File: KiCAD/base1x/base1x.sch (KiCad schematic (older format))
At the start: 39 parts, among them J1 Conn_02x05_Odd_Even, J2 GS3, J3 Conn_02x14_Counter_Clockwise, J4 GS3, J6 Conn_02x14_Counter_Clockwise, J7 Conn_02x06_Counter_Clockwise, J8 Conn_02x06_Counter_Clockwise, J9 Screw_Terminal_01x08, P3 CONN_01X02, P4 CONN_01X02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

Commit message: update kicad and add logos
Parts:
- J9: symbol Connector_Specialized:Screw_Terminal_01x08 -> Connector:Screw_Terminal_01x08
- L1: value GREY@CHRISTOFORO.NET -> grey@mutovis.com; footprint myParts:logo -> logo:logo_and_text; symbol myParts:GREY@CHRISTOFORO.NET -> logo:logo_text
- MK1, MK2: symbol Mechanical:Mounting_Hole_PAD -> Mechanical:MountingHole_Pad
- MK3, MK4, MK5, MK6, MK7, MK8: symbol Mechanical:Mounting_Hole -> Mechanical:MountingHole_Pad
- TP1, TP2, TP3, TP4, TP5, TP6: symbol Connector_Specialized:Test_Point -> Connector:TestPoint
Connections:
- no-connect marks 35 -> 41
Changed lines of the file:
@@
 V+
 $Comp
-L myParts:GREY@CHRISTOFORO.NET L1
+L logo:logo_text L1
 U 1 1 59B41702
-P 8950 7250
-F 0 "L1" H 8950 7125 60  0001 C CNN
-F 1 "GREY@CHRISTOFORO.NET" H 8950 7250 100 0000 C CNB
-F 2 "myParts:logo" H 8950 7250 60  0001 C CNN
-F 3 "" H 8950 7250 60  0001 C CNN
-	1    8950 7250
+P 9050 6800
+F 0 "L1" H 9050 6675 60  0001 C CNN
+F 1 "grey@mutovis.com" H 9000 6550 100 0000 C CNN
+F 2 "logo:logo_and_text" H 9050 6800 60  0001 C CNN
+F 3 "" H 9050 6800 60  0001 C CNN
+	1    9050 6800
 	1    0    0    -1
 $EndComp
@@
 External Power
 $Comp
-L Mechanical:Mounting_Hole_PAD MK1
+L Mechanical:MountingHole_Pad MK1
 U 1 1 59C916FE
 P 3300 6100
@@
 $EndComp
 $Comp
-L Mechanical:Mounting_Hole_PAD MK2
+L Mechanical:MountingHole_Pad MK2
 U 1 1 59C91760
 P 3300 6450
@@
 V_D_EXT
 $Comp
-L Connector_Specialized:Test_Point TP1
+L Connector:TestPoint TP1
 U 1 1 5A00C70E
 P 5650 6300
@@
 ~CS0
 $Comp
-L Connector_Specialized:Test_Point TP2
+L Connector:TestPoint TP2
 U 1 1 5A00C0AD
 P 4700 1850
@@
 I-R
 $Comp
-L Mechanical:Mounting_Hole MK3
+L Mechanical:MountingHole_Pad MK3
 U 1 1 5A00CBDC
 P 8800 1700
@@
 $EndComp
 $Comp
-L Mechanical:Mounting_Hole MK4
+L Mechanical:MountingHole_Pad MK4
 U 1 1 5A00CCA4
 P 8800 2050
@@
 $EndComp
 $Comp
-L Mechanical:Mounting_Hole MK5
+L Mechanical:MountingHole_Pad MK5
 U 1 1 5A00CCFE
 P 8800 2350
@@
 $EndComp
 $Comp
-L Mechanical:Mounting_Hole MK6
+L Mechanical:MountingHole_Pad MK6
 U 1 1 5A00CD58
 P 8800 2650
@@
 $EndComp
 $Comp
-L Mechanical:Mounting_Hole MK7
+L Mechanical:MountingHole_Pad MK7
 U 1 1 5A00CDAE
 P 8800 3000
@@
 $EndComp
 $Comp
-L Mechanical:Mounting_Hole MK8
+L Mechanical:MountingHole_Pad MK8
 U 1 1 5A00CE0E
 P 8800 3300
@@
 	4700 6750 4700 6450
 $Comp
-L Connector_Specialized:Screw_Terminal_01x08 J9
+L Connector:Screw_Terminal_01x08 J9
 U 1 1 5A36A6E7
 P 10150 1350
@@
 NoConn ~ 10050 1150
 $Comp
-L Connector_Specialized:Test_Point TP3
+L Connector:TestPoint TP3
 U 1 1 5A3700D5
 P 4250 2100
@@
 $EndComp
 $Comp
-L Connector_Specialized:Test_Point TP4
+L Connector:TestPoint TP4
 U 1 1 5A370173
 P 5000 2850
@@
 	5150 1200 4650 1200
 $Comp
-L Connector_Specialized:Test_Point TP5
+L Connector:TestPoint TP5
 U 1 1 5A371768
 P 5150 1200
@@
 This ADC will become ADS122C04 when it comes\nout to support analog inputs more negative than GND\nand I_sense will connect to AIN1
 $Comp
-L Connector_Specialized:Test_Point TP6
+L Connector:TestPoint TP6
 U 1 1 5A58BDB1
 P 10100 3850
@@
 Wire Wire Line
 	7250 2050 7500 2050
+NoConn ~ 8800 3400
+NoConn ~ 8800 3100
+NoConn ~ 8800 2750
+NoConn ~ 8800 2450
+NoConn ~ 8800 2150
+NoConn ~ 8800 1800
 $EndSCHEMATC

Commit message: MIT redesign in progress
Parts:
- removed J2, J4: GS3, Jumper:SolderJumper-3_P1.3mm_Open_RoundedPad1.0x1.5mm_NumberLabels, symbol Jumper:SolderJumper_3_Open
- removed JP2, JP3, JP4, JP5, JP6: Jumper_NO_Small, Jumper:SolderJumper-2_P1.3mm_Open_RoundedPad1.0x1.5mm, symbol Device:Jumper_NO_Small
- removed P3, P4: CONN_01X02, Connector_PinHeader_2.54mm:PinHeader_1x02_P2.54mm_Vertical, symbol Connector_Generic:Conn_01x02
- removed R5: 1, Resistor_SMD:R_2512_6332Metric, symbol Device:R
- removed U1: ADS1115, Package_SO:MSOP-10_3x3mm_P0.5mm, symbol myParts:ADS1115
- added C10, C9: 10uF, Capacitor_SMD:C_1206_3216Metric, symbol Device:C_Small
- added C11, C4, C7: 1000pF, Capacitor_SMD:C_1206_3216Metric, symbol Device:C_Small
- added C12, C13: 47uF, symbol Device:CP1_Small
- added C2, C3, C5, C6, C8: 0.1uF, Capacitor_SMD:C_1206_3216Metric, symbol Device:C_Small
- added J10, J11, J12, J13, J14, J16, J17, J2, J4, J5: Conn_01x03, symbol Connector_Generic:Conn_01x03
- added J15: Conn_01x08, symbol Connector_Generic:Conn_01x08
- added JP1, JP2: Jumper_NC_Small, Jumper:SolderJumper-2_P1.3mm_Open_RoundedPad1.0x1.5mm, symbol Device:Jumper_NC_Small
- added U2, U5: ads122c04, symbol myParts:ads122c04
- added U3, U6, U7: AD8615, Package_TO_SOT_SMD:TSOT-23-5, symbol Amplifier_Operational:AD8603
- added U4: NUP4202, Package_TO_SOT_SMD:SOT-363_SC-70-6, symbol Power_Protection:NUP4202
- added U8: LT1963AxQ-2.5, Package_TO_SOT_SMD:TO-263-5_TabPin3, symbol Regulator_Linear:LT1963AxQ-2.5
- added U9: LT3015xQ-2.5, Package_TO_SOT_SMD:TO-263-5_TabPin3, symbol Regulator_Linear:LT3015xQ-2.5
- C1: value 1uF -> 0.1uF
- D1, D2: C_D (none) -> 580pF; I_max (none) -> 20mA
- R1: value 1.2K -> 100R; farnellCode 2073370 -> 2073607
- R2: value 1.2K -> 100R; farnellCode 2073370 -> 2476379
- R3: value 10K -> 100R; farnellCode 2073607 -> 2476379
- R4: value 10K -> 2000R; farnellCode 2073607 -> 2476379
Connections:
- net labels added: +2V5, +5VA, -2V5, -5VA, GNDREF, V_Current, V_D1, V_D2
- net labels removed: I_sense, V_D_EXT, V_D_LOC
- wire segments 99 -> 247
- no-connect marks 41 -> 57
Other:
- note added: "Bias Voltage"
- note added: "Current Sense TIA"
- note added: "TRACO POWER TMR 6-0521"
- note removed: "Current Sense Resistor"
- note removed: "This ADC will become ADS122C04 when it comes\nout to support analog inputs more negative than GND\nand I_sense will connect to AIN1"
- moved on the sheet: D1, D2, J1, J7, J8, J9, MK1, MK2, MK3, MK4, MK5, MK6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

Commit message: base 1x revisions
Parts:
- removed J16: Conn_01x03, symbol Connector_Generic:Conn_01x03
- removed R4: 2000R, Resistor_SMD:R_1206_3216Metric, symbol Device:R_Small
- removed U4: NUP4202, Package_TO_SOT_SMD:SOT-363_SC-70-6, symbol Power_Protection:NUP4202
- added D10, D3, D4, D5, D6, D7, D8, D9: FDH333, Diode_THT:D_DO-35_SOD27_P7.62mm_Horizontal, symbol Diode:1N4148
- added J18, J19: Conn_01x03, symbol Connector_Generic:Conn_01x03
- added JP3: Jumper_NO_Small, symbol Device:Jumper_NO_Small
- added MK10, MK11, MK12, MK13, MK14, MK9: Mounting_Hole, MountingHole:MountingHole_3.2mm_M3, symbol Mechanical:MountingHole_Pad
- added R10, R11, R9: 50R, Resistor_SMD:R_1206_3216Metric, symbol Device:R_Small
- added R5, R7: 900k, Resistor_SMD:R_1206_3216Metric, symbol Device:R_Small
- added R6, R8: 100k, Resistor_SMD:R_1206_3216Metric, symbol Device:R_Small
- R1: value 100R -> 20R
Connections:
- net +2V5: now also R5.2, R7.2
- net -2V5: no longer D1.2 (A), D2.2 (A), U6.2 (V-), U7.2 (V-)
- net GNDREF: now also D1.2 (A), D2.2 (A), J14.1 (Pin_1), U6.2 (V-), U7.2 (V-), R6.1, R8.1; no longer U6.4 (-), U7.4 (-)
- net I+: now also J18.2 (Pin_2), J19.2 (Pin_2)
- net I-_EXT: now also D10.1 (K), D9.2 (A)
- net V_Current: now also R11.1; no longer U2.10 (AIN1)
- net V_D1: now also R10.1; no longer C11.2, R3.1, TP3.1, U7.1
- net V_D2: now also R9.1; no longer C7.2, R2.1, TP4.1, U6.1
- net Vin: now also JP3.1; no longer J1.9 (Pin_9)
- net EnableTraco: now reaches J1.5 (Pin_5)
- net EnableTraco: now also J15.3 (Pin_3)
- net at C11.1, D1.1 (K), R3.2: now also U7.4 (-); no longer U7.3 (+)
- net at C7.1, D2.1 (K), R2.2: now also U6.4 (-); no longer U6.3 (+)
- net at C4.1, J4.3 (Pin_3), R1.2: now also U3.4 (-); no longer U3.3 (+)
- net at J2.2 (Pin_2): now also U3.3 (+); no longer U3.4 (-)
- new net: J1.9 (Pin_9), JP3.2
- new net: C7.2, R2.1, R9.2, TP4.1, U6.1
- new net: R5.1, R6.2, U6.3 (+)
- new net: R7.1, R8.2, U7.3 (+)
- new net: C11.2, R10.2, R3.1, TP3.1, U7.1
- new net: R11.2, U2.10 (AIN1)
- new net: D3.1 (K), J18.1 (Pin_1)
- new net: D3.2 (A), D5.1 (K)
- new net: D5.2 (A), D7.1 (K)
- new net: D7.2 (A), D9.1 (K)
- new net: D10.2 (A), D8.1 (K)
- new net: D6.1 (K), D8.2 (A)
- new net: D4.1 (K), D6.2 (A)
- new net: D4.2 (A), J19.1 (Pin_1)
- no-connect marks 57 -> 62
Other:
- note added: "Arduino Mounts"
- note added: "Controller Mounts"
- note added: "Diagnose I+"
- note added: "Diagnose I-"
- note added: "Diagnose V+"
- note added: "Diagnose V-"
- note added: "Disable TIA"
- note added: "FDH333 : 500mA of protection, 2x3nA of leakage\nTZX2V7A : 185mA, 5uA\nMUR120-T : 1000mA, 2uA"
- note added: "Float I-"
- note added: "Gain=20V/A"
- note added: "Molex Vin Select"
- note added: "Overvoltage Protection"
- note added: "Pi Mounts"
- note added: "Protect"
- note added: "The Ds here could optionally be 2x TZX2V7A or 8x MUR120-T"
- note added: "Tie Grounds"
- note added: "Transimpedance Current Amplifier"
- note added: "Use External TIA GND"
- note removed: "POWER FLAGS"
- moved on the sheet: C1, C11, C2, C3, C4, C7, D1, D2, J1, J13, J14, J15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

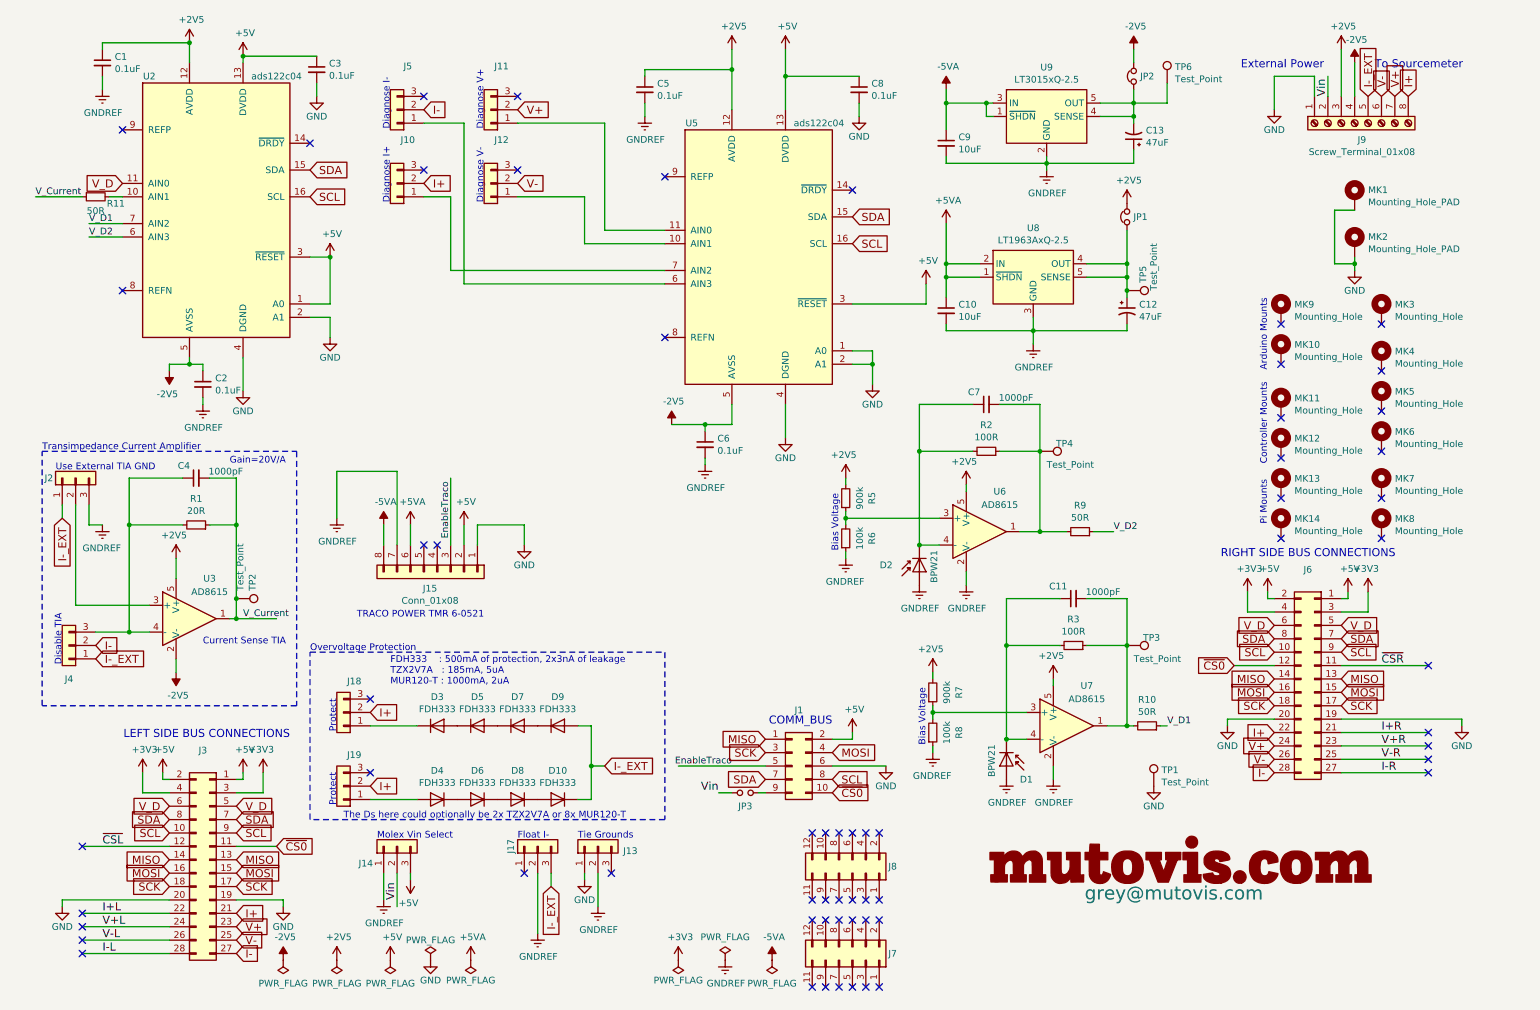
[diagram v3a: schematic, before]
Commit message: fix up bus connections
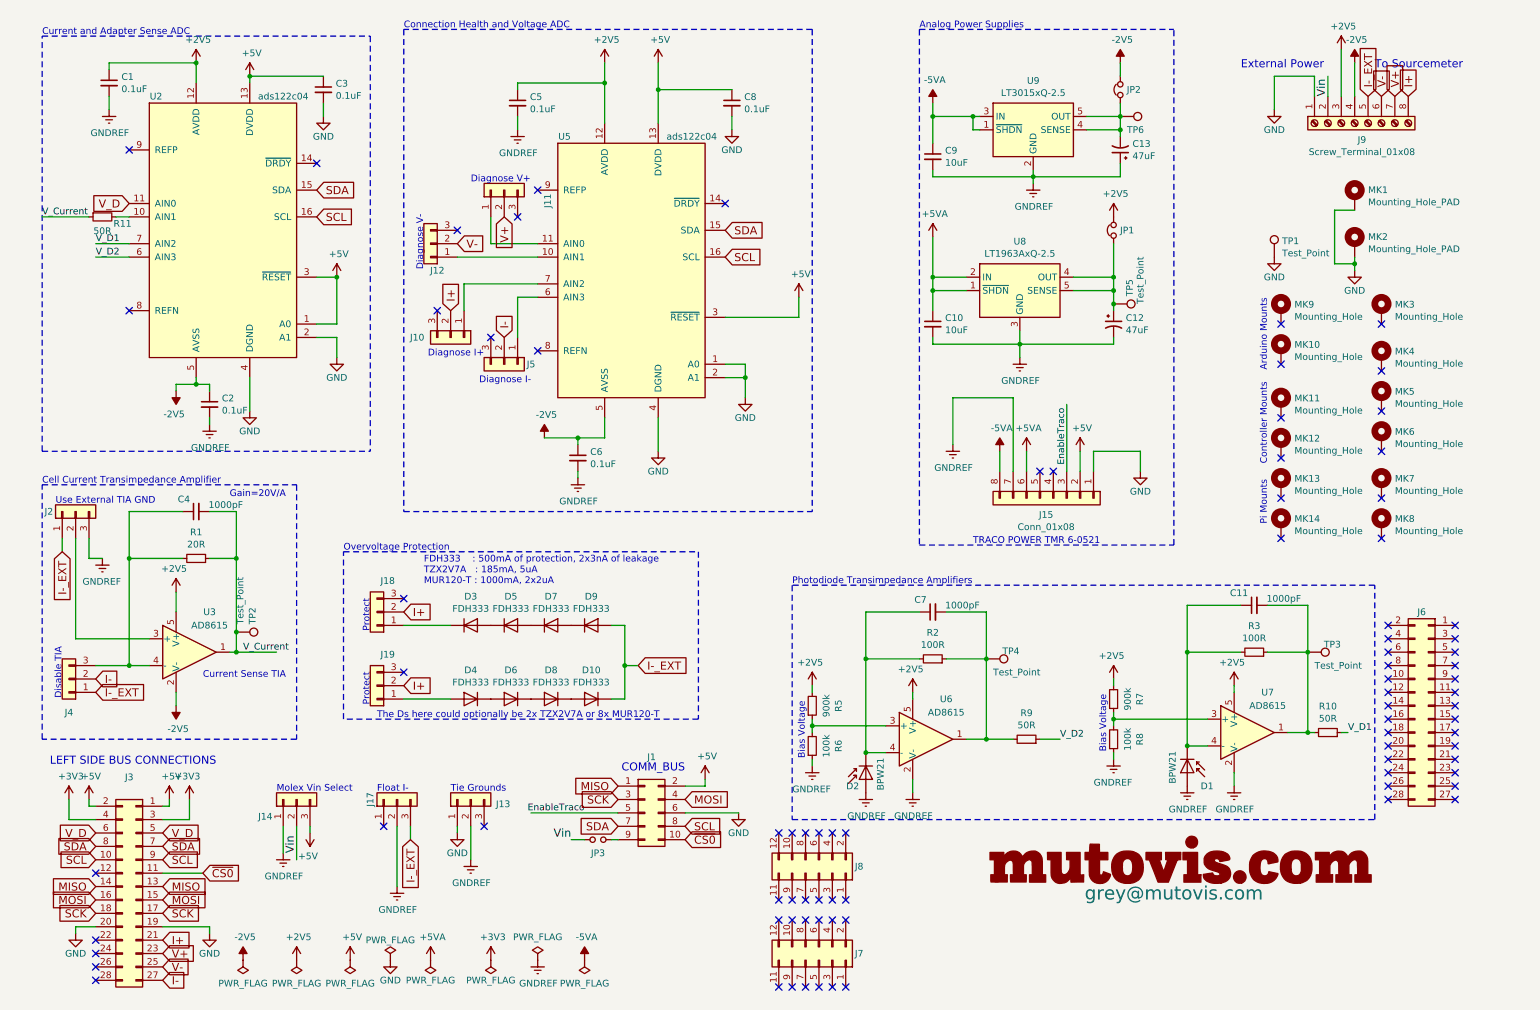
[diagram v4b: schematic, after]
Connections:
- net +3V3: no longer J6.3 (Pin_3), J6.4 (Pin_4)
- net +5V: no longer J6.1 (Pin_1), J6.2 (Pin_2)
- net GND: no longer J6.19 (Pin_19), J6.20 (Pin_20)
- net I+: no longer J6.22 (Pin_22)
- net I-: no longer J6.28 (Pin_28)
- net MISO: no longer J6.13 (Pin_13), J6.14 (Pin_14)
- net MOSI: no longer J6.15 (Pin_15), J6.16 (Pin_16)
- net SCK: no longer J6.17 (Pin_17), J6.18 (Pin_18)
- net SCL: no longer J6.10 (Pin_10), J6.9 (Pin_9)
- net SDA: no longer J6.7 (Pin_7), J6.8 (Pin_8)
- net V+: no longer J6.24 (Pin_24)
- net V-: no longer J6.26 (Pin_26)
- net V_D: no longer J6.5 (Pin_5), J6.6 (Pin_6)
- net ~CS0: no longer J6.12 (Pin_12)
- net I+L: no longer names the net of J3.22 (Pin_22)
- net I+R: no longer names the net of J6.21 (Pin_21)
- net I-L: no longer names the net of J3.28 (Pin_28)
- net I-R: no longer names the net of J6.27 (Pin_27)
- net V+L: no longer names the net of J3.24 (Pin_24)
- net V+R: no longer names the net of J6.23 (Pin_23)
- net V-L: no longer names the net of J3.26 (Pin_26)
- net V-R: no longer names the net of J6.25 (Pin_25)
- net ~CSL: no longer names the net of J3.12 (Pin_12)
- net ~CSR: no longer names the net of J6.11 (Pin_11)
- no-connect marks 62 -> 85
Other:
- note added: "Analog Power Supplies"
- note added: "Cell Current Transimpedance Amplifier"
- note added: "Connection Health and Voltage ADC"
- note added: "Current and Adapter Sense ADC"
- note added: "FDH333 : 500mA of protection, 2x3nA of leakage\nTZX2V7A : 185mA, 5uA\nMUR120-T : 1000mA, 2x2uA"
- note added: "Photodiode Transimpedance Amplifiers"
- note removed: "FDH333 : 500mA of protection, 2x3nA of leakage\nTZX2V7A : 185mA, 5uA\nMUR120-T : 1000mA, 2uA"
- note removed: "RIGHT SIDE BUS CONNECTIONS"
- note removed: "Transimpedance Current Amplifier"
- moved on the sheet: C1, C10, C11, C12, C13, C2, C3, C4, C5, C6, C7, C8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

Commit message: cut right mux connector in half
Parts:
- J6: symbol Connector_Generic:Conn_02x14_Odd_Even -> Connector_Generic:Conn_01x14
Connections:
- no-connect marks 85 -> 71
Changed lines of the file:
@@
 V_D
 $Comp
-L Connector_Generic:Conn_02x14_Odd_Even J6
+L Connector_Generic:Conn_01x14 J6
 U 1 1 59C14E79
 P 10900 5650
@@
 NoConn ~ 11100 5150
 NoConn ~ 11100 5050
-NoConn ~ 10600 6350
-NoConn ~ 10600 6250
-NoConn ~ 10600 6150
-NoConn ~ 10600 6050
-NoConn ~ 10600 5950
-NoConn ~ 10600 5850
-NoConn ~ 10600 5750
-NoConn ~ 10600 5650
-NoConn ~ 10600 5550
-NoConn ~ 10600 5450
-NoConn ~ 10600 5350
-NoConn ~ 10600 5250
-NoConn ~ 10600 5150
-NoConn ~ 10600 5050
 Connection ~ 6700 6000
 Wire Wire Line

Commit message: work sync
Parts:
- added TP7: Test_Point, myParts:Test_Point_S1751-46R, symbol Connector:TestPoint
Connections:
- net GNDREF: now also TP7.1
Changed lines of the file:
@@
 NoConn ~ 950  7400
 NoConn ~ 950  6900
+$Comp
+L Connector:TestPoint TP7
+U 1 1 5C3E8296
+P 9750 1850
+F 0 "TP7" H 9808 1970 50  0000 L CNN
+F 1 "Test_Point" H 9808 1879 50  0000 L CNN
+F 2 "myParts:Test_Point_S1751-46R" H 9950 1850 50  0001 C CNN
+F 3 "" H 9950 1850 50  0001 C CNN
+F 4 "2293786" H 4100 -4450 50  0001 C CNN "farnellCode"
+	1    9750 1850
+	1    0    0    -1
+$EndComp
+$Comp
+L power:GNDREF #PWR022
+U 1 1 5C3F39DD
+P 9750 1850
+F 0 "#PWR022" H 9750 1600 50  0001 C CNN
+F 1 "GNDREF" H 9755 1677 50  0000 C CNN
+F 2 "" H 9750 1850 50  0001 C CNN
+F 3 "" H 9750 1850 50  0001 C CNN
+	1    9750 1850
+	1    0    0    -1
+$EndComp
 $EndSCHEMATC
